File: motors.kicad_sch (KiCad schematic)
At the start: 32 parts, among them Q1 NMOS, Q2 NMOS, Q3 NMOS, Q4 NMOS

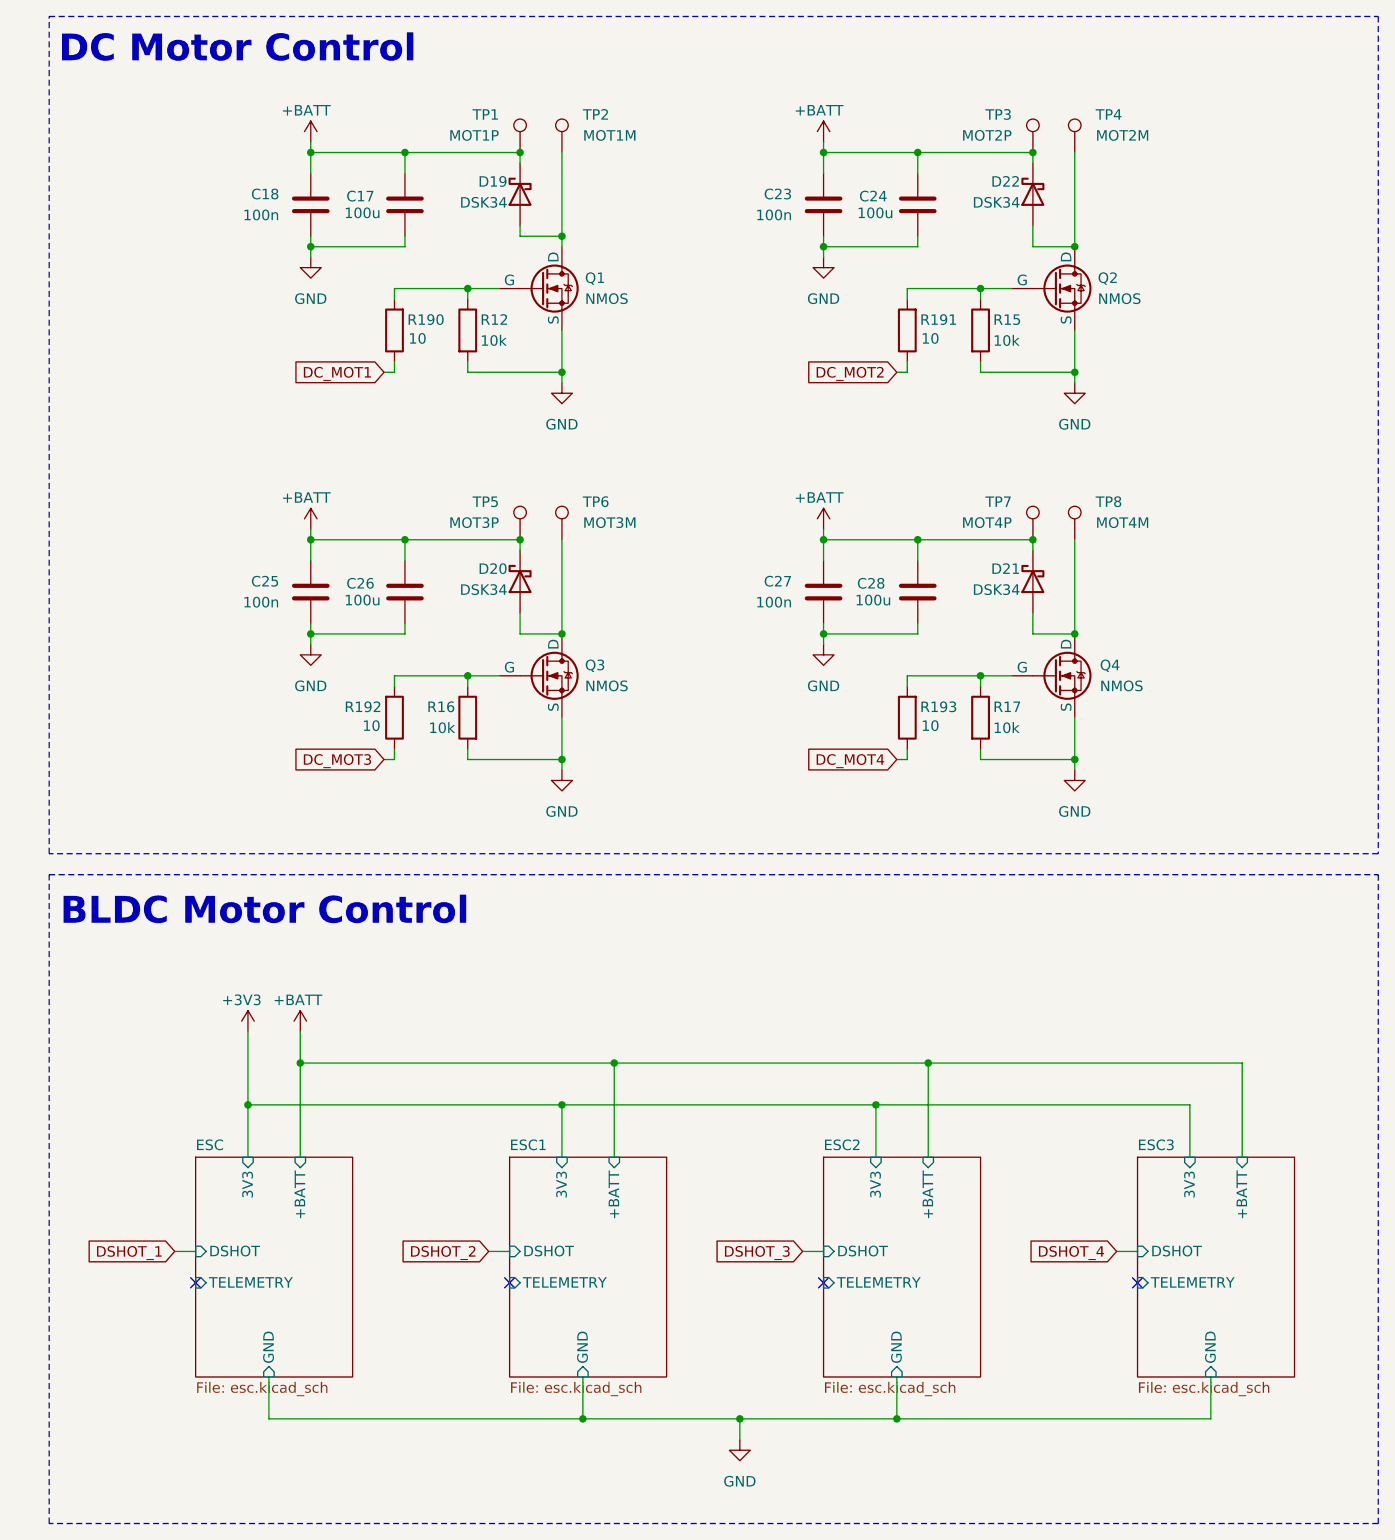
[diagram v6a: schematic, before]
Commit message: Reset schematic part number annotations
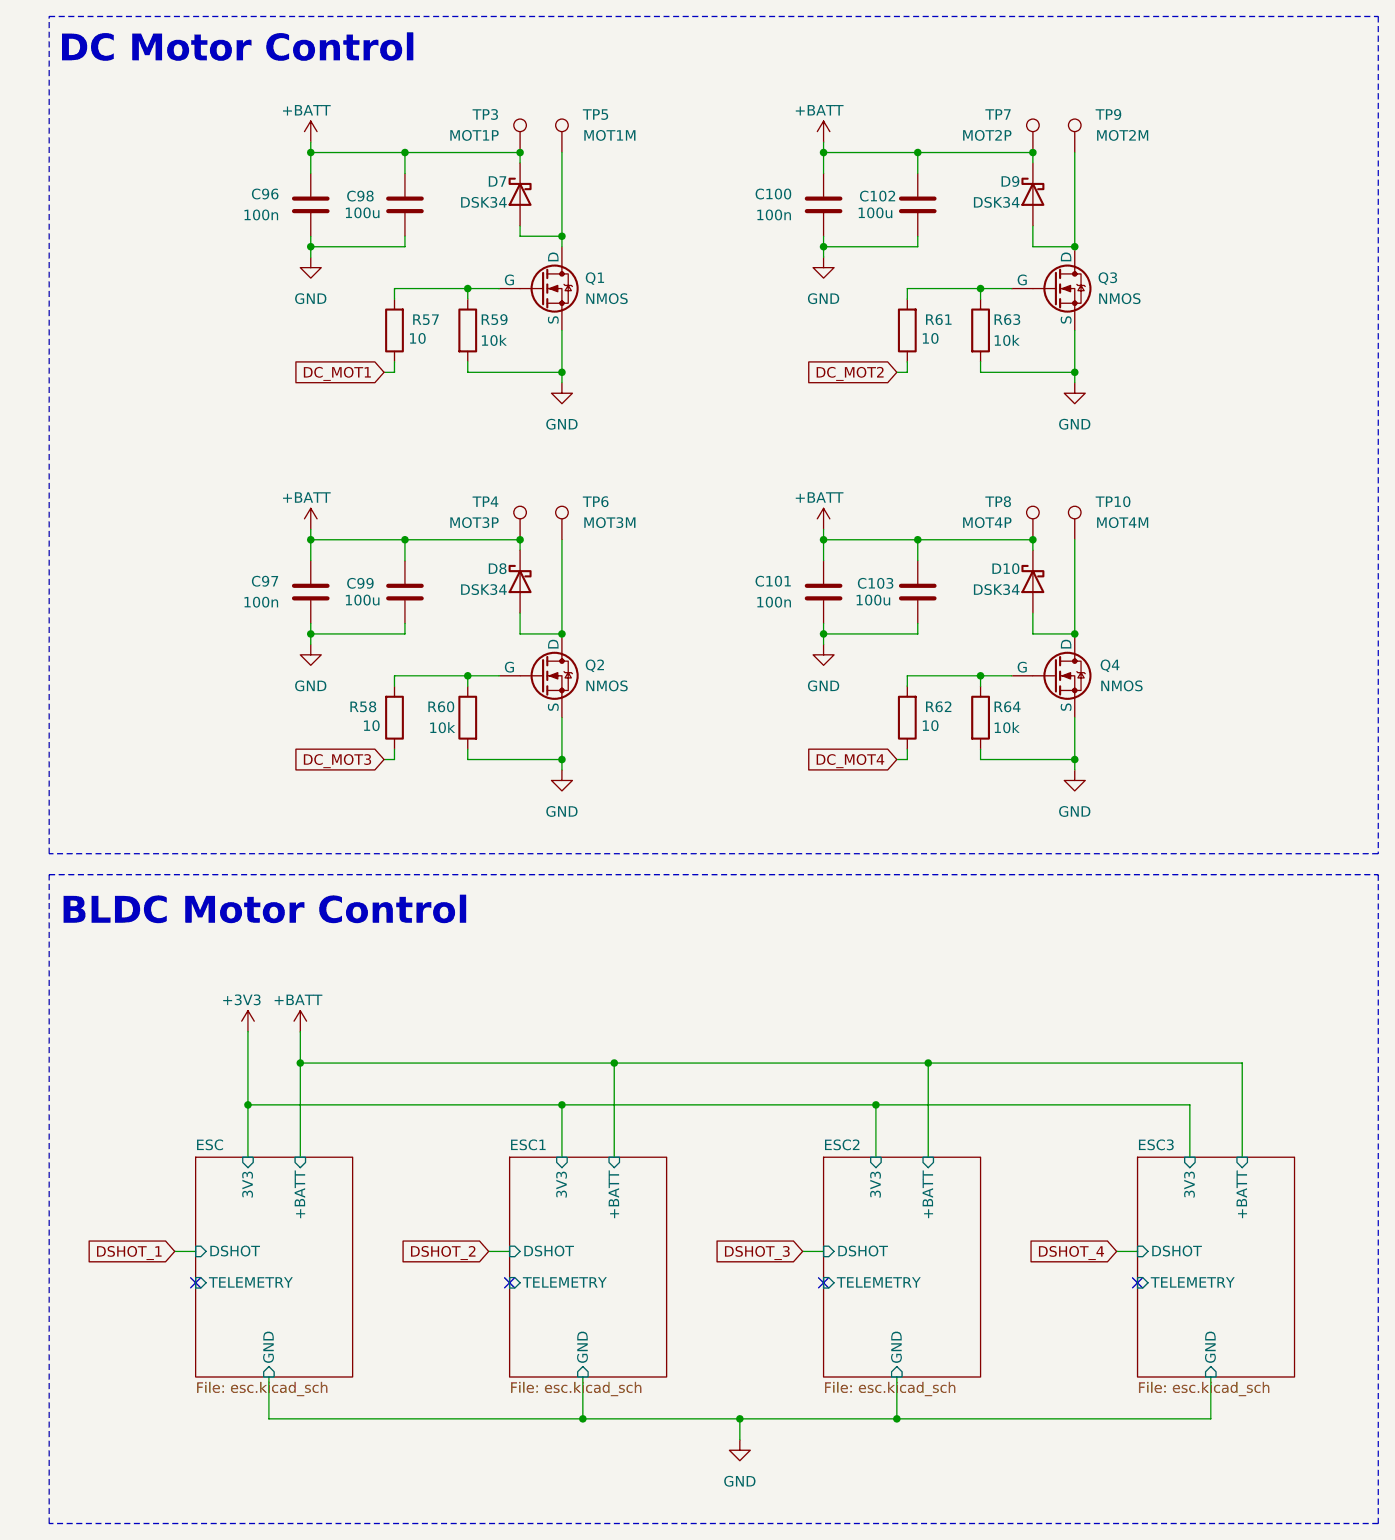
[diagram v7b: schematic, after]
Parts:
- renumbered C23 to C100, C27 to C101, C24 to C102, C28 to C103, C18 to C96, C25 to C97, C17 to C98, C26 to C99, D21 to D10, D19 to D7, D20 to D8, D22 to D9, Q3 to Q2, Q2 to Q3, R190 to R57, R192 to R58, R12 to R59, R16 to R60, R191 to R61, R193 to R62, R15 to R63, R17 to R64, TP8 to TP10, TP1 to TP3, TP5 to TP4, TP2 to TP5, TP3 to TP7, TP7 to TP8, TP4 to TP9

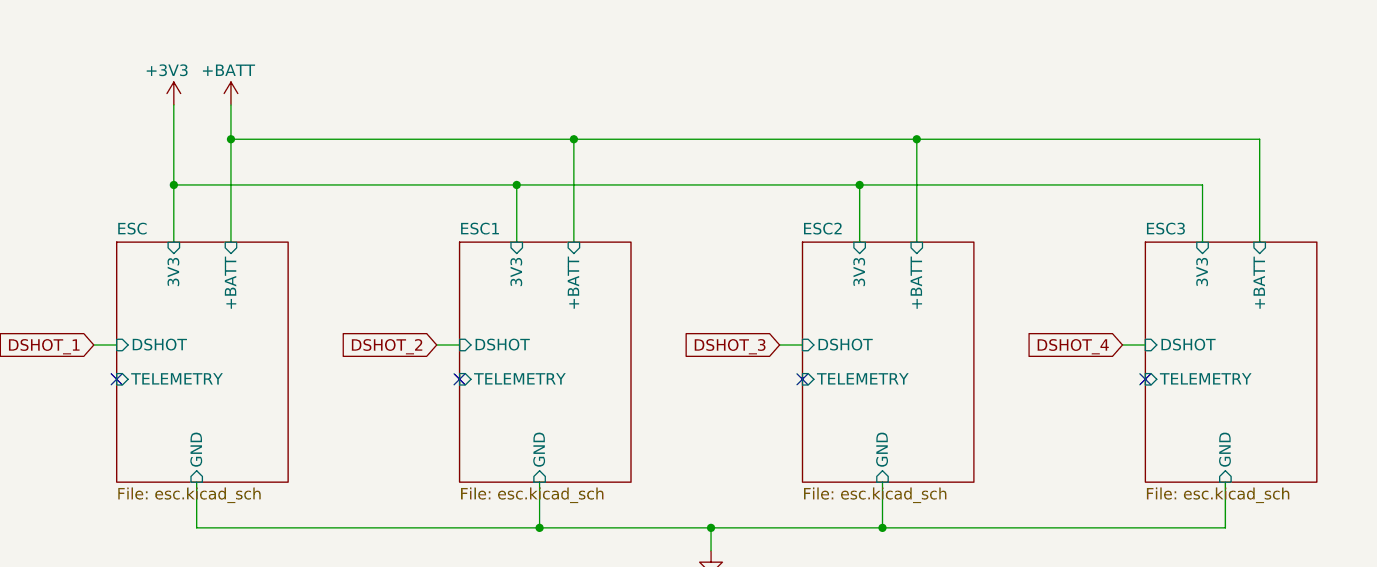
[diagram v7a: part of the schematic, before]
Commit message: Fix ERC errors
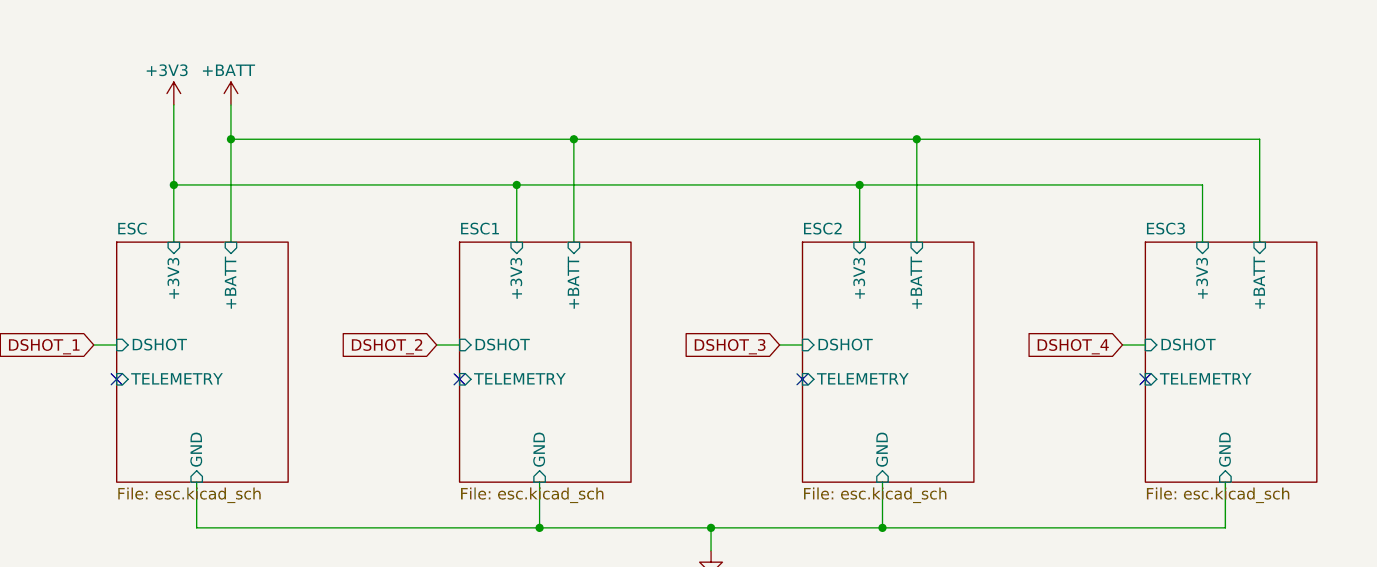
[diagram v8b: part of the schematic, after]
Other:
- sheet ESC ports: added +3V3; removed 3V3
- sheet ESC1 ports: added +3V3; removed 3V3
- sheet ESC2 ports: added +3V3; removed 3V3
- sheet ESC3 ports: added +3V3; removed 3V3
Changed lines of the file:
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@@
-			)
-		)
-		(pin "3V3" input
-			(at 76.2 152.4 90)
-			(effects
-				(font
-					(size 1.27 1.27)
-				)
-				(justify right)
 			)
 		)
@@
 				)
 				(justify left)
+			)
+		)
+		(pin "+3V3" input
+			(at 76.2 152.4 90)
+			(effects
+				(font
+					(size 1.27 1.27)
+				)
+				(justify right)
 			)
 		)
@@
 			)
 		)
-		(pin "3V3" input
+		(pin "+3V3" input
 			(at 152.4 152.4 90)
 			(effects
@@
 			)
 		)
-		(pin "3V3" input
+		(pin "+3V3" input
 			(at 114.3 152.4 90)
 			(effects
@@
 			)
 		)
-		(pin "3V3" input
+		(pin "+3V3" input
 			(at 38.1 152.4 90)
 			(effects
